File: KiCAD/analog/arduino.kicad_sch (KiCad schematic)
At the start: 42 parts, among them J11 Screw_Terminal_01x03, J12 Screw_Terminal_01x04, J13 Screw_Terminal_01x03, J14 Screw_Terminal_01x05, J16 Screw_Terminal_01x03, J17 Conn_Coaxial_Small, J18 Conn_Coaxial_Small, J19 Conn_Coaxial_Small, J20 Screw_Terminal_01x04, J21 Screw_Terminal_01x02, J22 Screw_Terminal_01x04, J6 Screw_Terminal_01x02, J7 Screw_Terminal_01x02, J8 Screw_Terminal_01x02, J9 TR_SENSE, Q4 2N7000, Q5 2N7000, Q6 2N7000, Q7 2N7000, U1 MCP1700x-330xxTO, U17 Adafruit_PCF8575_Breakout, U18 CD14538B, U2 Metro_ESP32S3

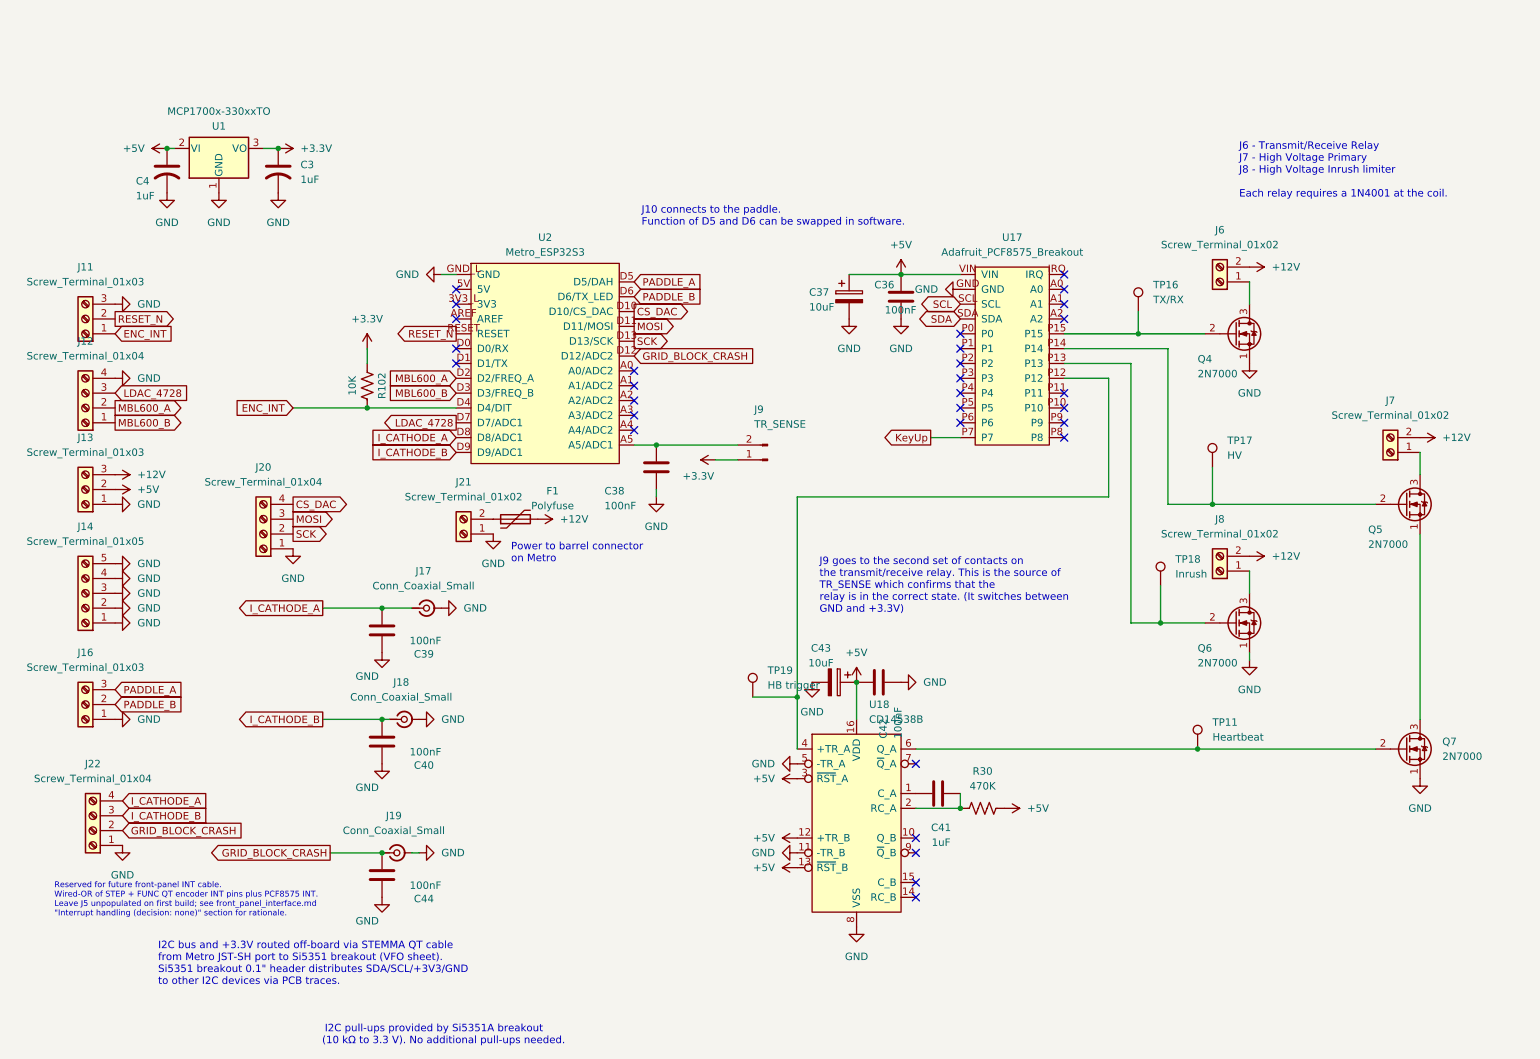
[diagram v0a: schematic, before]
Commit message: revB: arduino screw terminals + bias schematic edits; grid_bias.md updated for MCP4728 internal reference
Analog board arduino sheet: added screw terminal connections for all Metro GPIO
signals (PADDLE_A/B, I_CATHODE_A/B, GRID_BLOCK_CRASH, ENC_INT, MBL600_A/B).
Bias board: schematic edits (session work). grid_bias.md: corrected DAC codes
and rail voltages for MCP4728 internal 2.048V bandgap reference (OPERATE ~2667),
updated inter-sheet I/O references from MCP4725 to MCP4728.

Co-Authored-By: Claude Sonnet 4.6 <noreply@anthropic.com>
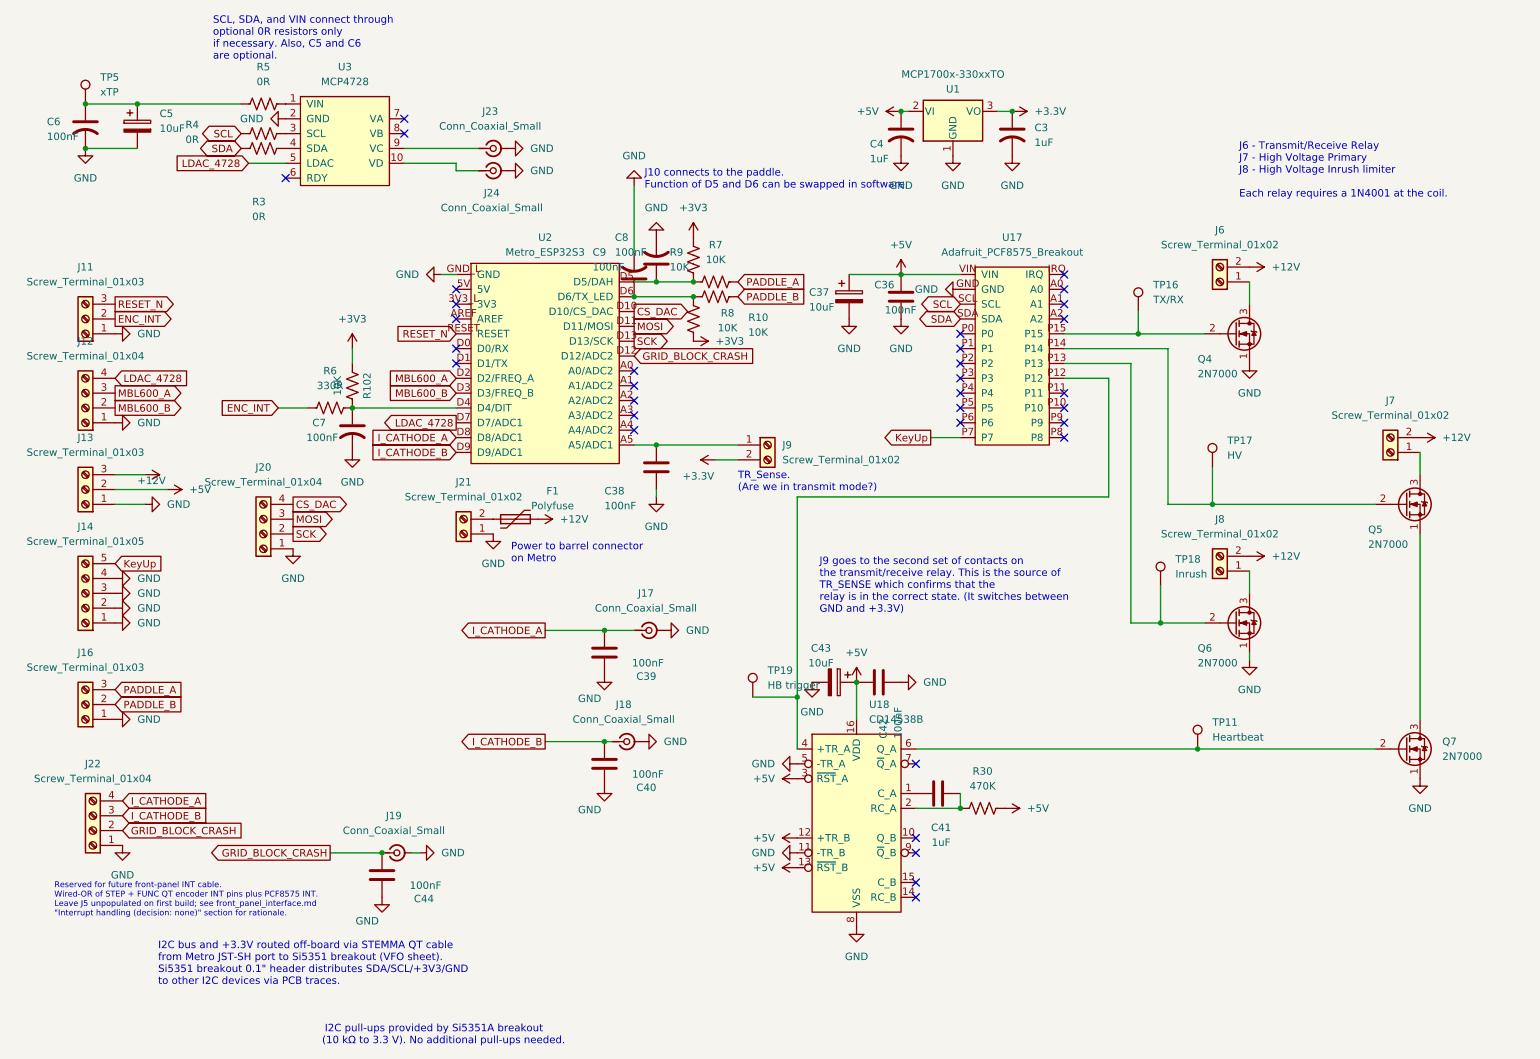
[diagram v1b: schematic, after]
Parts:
- removed J9: TR_SENSE, Connector_PinHeader_2.54mm:PinHeader_1x02_P2.54mm_Vertical, symbol Connector:Conn_01x02_Pin
- added C5: 10uF, symbol Device:C_Polarized
- added C6, C7, C8, C9: 100nF, symbol Device:C_US
- added J23, J24: Conn_Coaxial_Small, symbol Connector:Conn_Coaxial_Small
- added J9: Screw_Terminal_01x02, symbol Connector:Screw_Terminal_01x02
- added R10, R7, R8, R9: 10K, symbol Device:R_US
- added R3, R4, R5: 0R, symbol Device:R_US
- added R6: 330R, symbol Device:R_US
- added TP5: xTP, Connector_PinHeader_2.54mm:PinHeader_1x01_P2.54mm_Vertical, symbol xmitter:xTP
- added U3: MCP4728, symbol xmitter:MCP4728
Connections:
- net +3.3V: now also J9.2 (Pin_2); no longer R102.1
- net ENC_INT: now also J11.2 (Pin_2), R6.1; no longer J11.1 (Pin_1), R102.2, U2.D4 (D4/DIT)
- net GND: now also J11.1 (Pin_1), J12.1 (Pin_1), C5.2, C6.2, C7.2, C8.2, C9.2, J23.2 (Ext), J24.2 (Ext), U3.2 (GND); no longer J11.3 (Pin_3), J12.4 (Pin_4), J14.5 (Pin_5)
- net KeyUp: now also J14.5 (Pin_5)
- net LDAC_4728: now also J12.4 (Pin_4), U3.5 (LDAC); no longer J12.3 (Pin_3)
- net MBL600_A: now also J12.3 (Pin_3); no longer J12.2 (Pin_2)
- net MBL600_B: now also J12.2 (Pin_2); no longer J12.1 (Pin_1)
- net PADDLE_A: now also R7.2; no longer U2.D5 (D5/DAH)
- net PADDLE_B: now also R8.2; no longer U2.D6 (D6/TX_LED)
- net RESET_N: now also J11.3 (Pin_3); no longer J11.2 (Pin_2)
- net SCL: now also R4.1
- net SDA: now also R3.1
- net at C38.1, U2.A5 (A5/ADC1): now also J9.1 (Pin_1)
- new net: R5.2, U3.1 (VIN)
- new net: J24.1 (In), U3.10 (VD)
- new net: R4.2, U3.3 (SCL)
- new net: R3.2, U3.4 (SDA)
- new net: J23.1 (In), U3.9 (VC)
- new net: C7.1, R102.2, R6.2, U2.D4 (D4/DIT)
- new net: C8.1, R7.1, R9.1, U2.D5 (D5/DAH)
- new net: C9.1, R10.2, R8.1, U2.D6 (D6/TX_LED)
- new net: C5.1, C6.1, R5.1, TP5.1
- new net +3V3: R10.1, R102.1, R9.2
- no-connect marks 30 -> 33
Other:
- note added: "SCL, SDA, and VIN connect through optional 0R resistors only if necessary. Also, C5 and C6 are optional."
- note added: "TR_Sense. (Are we in transmit mode?)"
- moved on the sheet: C3, C39, C4, C40, J17, J18, R102, U1

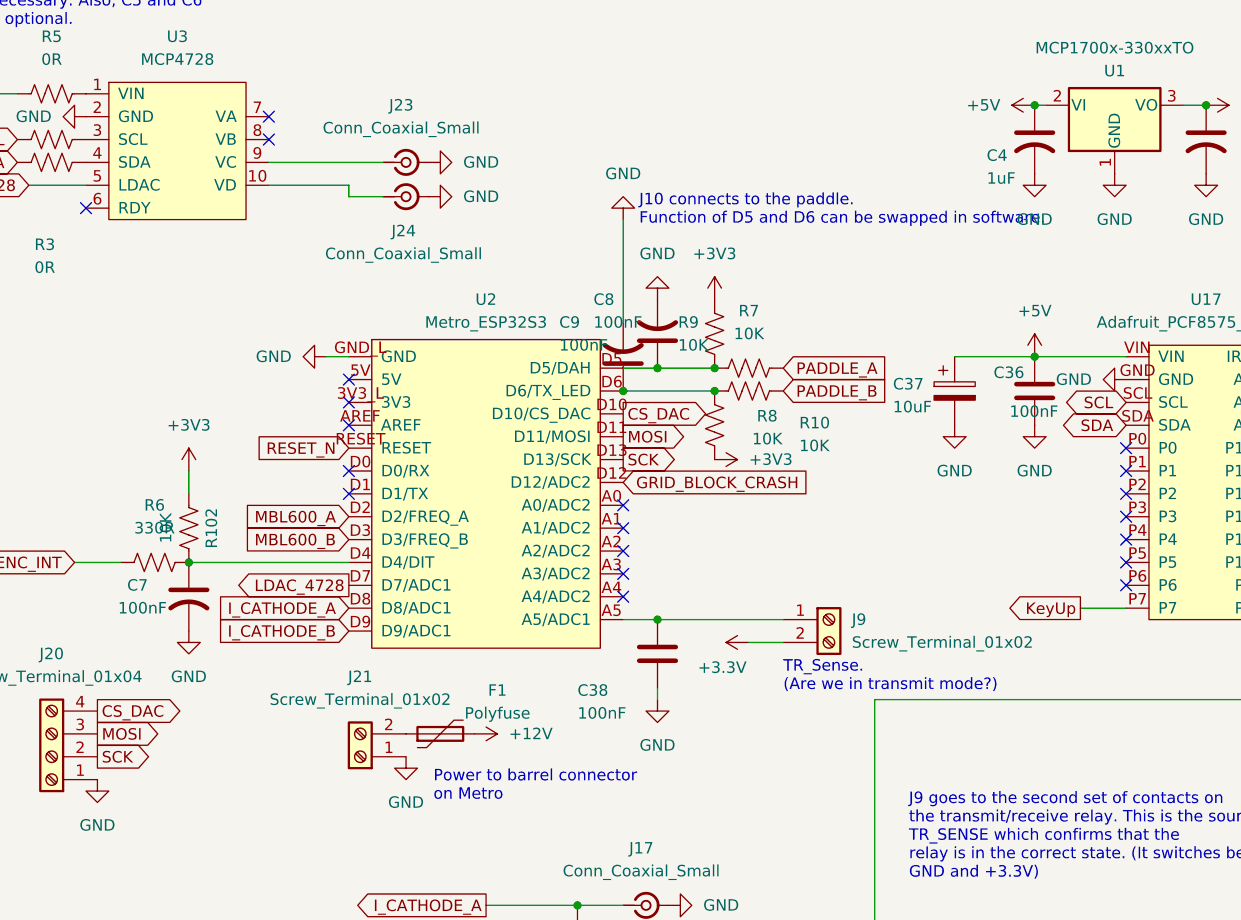
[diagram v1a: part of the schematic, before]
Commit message: revB: remove Metro/shield components from analog; stub power and protoshield projects
arduino.kicad_sch: deleted U2 (Metro ESP32-S3), bypass caps, series/pull-up
resistors, and associated labels — these move to the protoshield board.
Screw terminals retained as the analog-board boundary connectors.
KiCAD/protoshield/: new project stub for Metro-mounted protoboard (bypass,
series R, pull-ups connecting directly to Metro GPIO pins).
KiCAD/power/: new project stub for dedicated power board (bridge supply
migrating from analog; will add HV rectifier/filter for PA).

Co-Authored-By: Claude Sonnet 4.6 <noreply@anthropic.com>
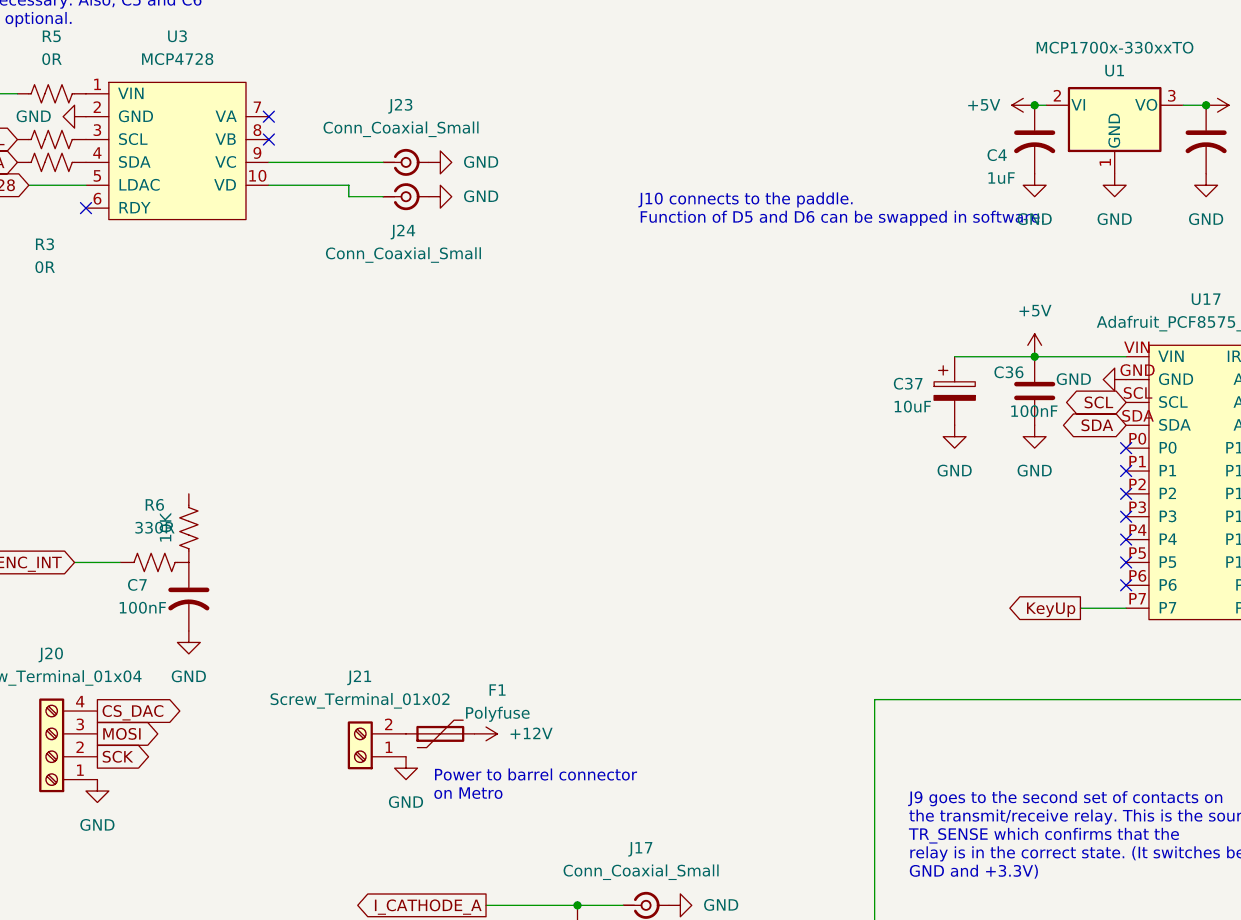
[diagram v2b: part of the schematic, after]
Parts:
- removed C38: 100nF, Capacitor_THT:C_Disc_D5.0mm_W2.5mm_P5.00mm, symbol Device:C
- removed C8, C9: 100nF, symbol Device:C_US
- removed J9: Screw_Terminal_01x02, symbol Connector:Screw_Terminal_01x02
- removed R10, R7, R8, R9: 10K, symbol Device:R_US
- removed U2: Metro_ESP32S3, symbol xmitter:Metro_ESP32S3
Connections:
- net +3V3: no longer names the net of R102.1
- no-connect marks 33 -> 23
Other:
- note removed: "TR_Sense. (Are we in transmit mode?)"
